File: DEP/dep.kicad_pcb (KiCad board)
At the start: 2 copper layers, 100 x 73 mm, 54 parts, among them J1 AudioJack2, J2 Barrel_Jack_Switch, J3 AudioJack2, J4 AudioJack2, J5 Conn_01x14, J6 Conn_01x14, J7 Conn_01x20, J8 Conn_01x20, U1 OPA2134, U2 PCM4201PWR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

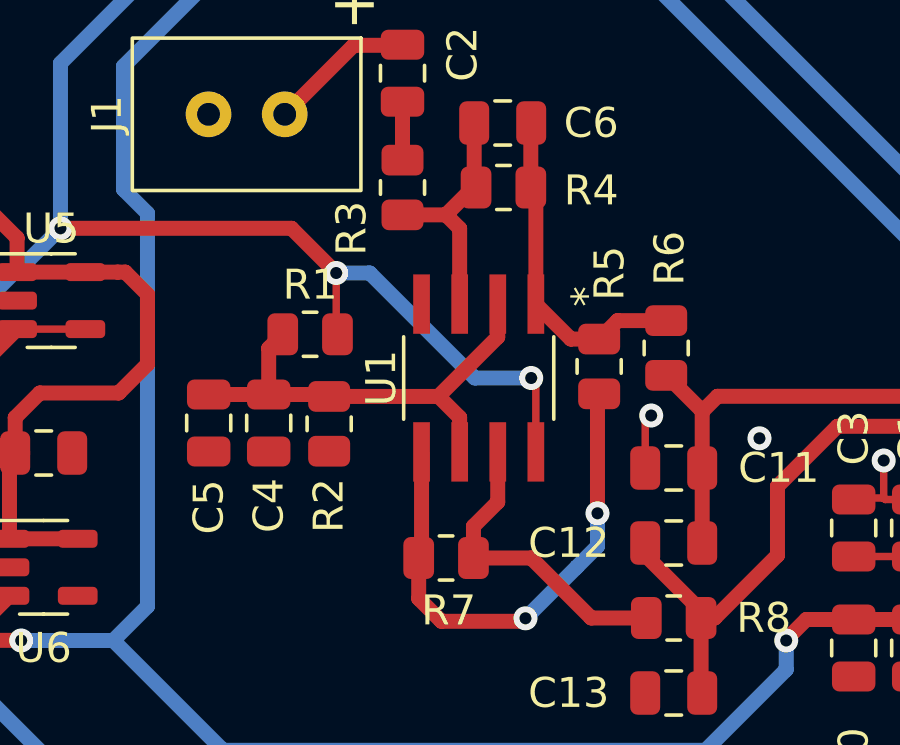
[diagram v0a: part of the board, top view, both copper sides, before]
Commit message: fix +/- op-amp error...
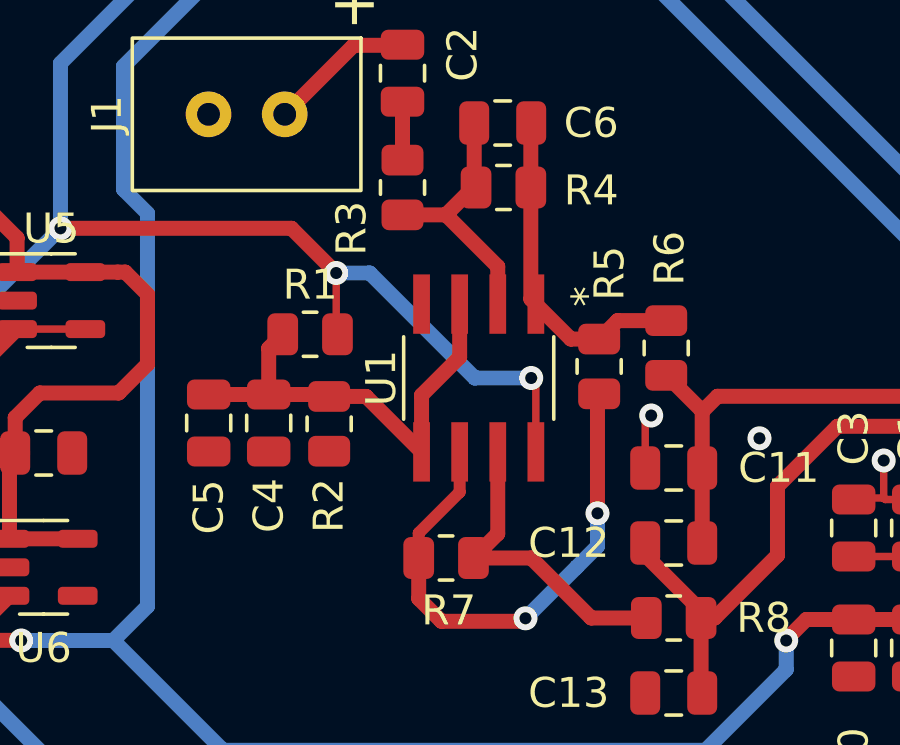
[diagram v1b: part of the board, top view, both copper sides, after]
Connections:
- U1 pad 2: /Input/2V5_reference_input_stage -> /Input/OPamp_1_positive_input
- U1 pad 3: /Input/OPamp_1_positive_input -> /Input/2V5_reference_input_stage
- U1 pad 5: /Input/OPamp_2_positive_input -> /Input/2V5_reference_input_stage
- U1 pad 6: /Input/2V5_reference_input_stage -> /Input/OPamp_2_positive_input
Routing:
- net /Input/OPamp_2_positive_input: track 17.3 -> 18.0 mm
- net /Input/OPamp_1_positive_input: track 8.07 -> 8.59 mm
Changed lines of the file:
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@@
       (net 31 "/Input/OPamp_1_output") (pintype "output"))
     (pad "2" smd rect (at -2.4638 -0.635 270) (size 1.9812 0.5588) (layers "F.Cu" "F.Paste" "F.Mask")
-      (net 29 "/Input/2V5_reference_input_stage") (pinfunction "-") (pintype "input"))
+      (net 30 "/Input/OPamp_1_positive_input") (pinfunction "-") (pintype "input"))
     (pad "3" smd rect (at -2.4638 0.635 270) (size 1.9812 0.5588) (layers "F.Cu" "F.Paste" "F.Mask")
-      (net 30 "/Input/OPamp_1_positive_input") (pinfunction "+") (pintype "input"))
+      (net 29 "/Input/2V5_reference_input_stage") (pinfunction "+") (pintype "input"))
     (pad "4" smd rect (at -2.4638 1.905 270) (size 1.9812 0.5588) (layers "F.Cu" "F.Paste" "F.Mask")
       (net 1 "GND") (pinfunction "V-") (pintype "power_in"))
     (pad "5" smd rect (at 2.4638 1.905 270) (size 1.9812 0.5588) (layers "F.Cu" "F.Paste" "F.Mask")
-      (net 32 "/Input/OPamp_2_positive_input") (pinfunction "+") (pintype "input"))
+      (net 29 "/Input/2V5_reference_input_stage") (pinfunction "+") (pintype "input"))
     (pad "6" smd rect (at 2.4638 0.635 270) (size 1.9812 0.5588) (layers "F.Cu" "F.Paste" "F.Mask")
-      (net 29 "/Input/2V5_reference_input_stage") (pinfunction "-") (pintype "input"))
+      (net 32 "/Input/OPamp_2_positive_input") (pinfunction "-") (pintype "input"))
     (pad "7" smd rect (at 2.4638 -0.635 270) (size 1.9812 0.5588) (layers "F.Cu" "F.Paste" "F.Mask")
       (net 33 "/Input/OPamp_2_output") (pintype "output"))
@@
   (segment (start 128.611 85.96) (end 125.254 85.96) (width 0.5) (layer "F.Cu") (net 28))
   (segment (start 128.86 85.96) (end 129.6 86.7) (width 0.5) (layer "F.Cu") (net 28))
-  (segment (start 140.006 90.806) (end 140.006 91.9538) (width 0.5) (layer "F.Cu") (net 29))
-  (segment (start 139.305 90.095) (end 141.276 88.124) (width 0.5) (layer "F.Cu") (net 29))
-  (segment (start 139.305 90.105) (end 140.006 90.806) (width 0.5) (layer "F.Cu") (net 29))
+  (segment (start 138.736 91.9538) (end 138.736 90.064) (width 0.5) (layer "F.Cu") (net 29))
   (segment (start 135.591 90.04) (end 135.656 90.105) (width 0.5) (layer "F.Cu") (net 29))
-  (segment (start 141.276 88.124) (end 141.276 87.0262) (width 0.5) (layer "F.Cu") (net 29))
-  (segment (start 139.305 90.105) (end 139.305 90.095) (width 0.5) (layer "F.Cu") (net 29))
   (segment (start 133.641 88.5) (end 134.1085 88.0325) (width 0.5) (layer "F.Cu") (net 29))
   (segment (start 133.641 90.04) (end 135.591 90.04) (width 0.5) (layer "F.Cu") (net 29))
+  (segment (start 140.006 88.794) (end 140.006 87.0262) (width 0.5) (layer "F.Cu") (net 29))
   (segment (start 133.641 90.04) (end 133.641 88.5) (width 0.5) (layer "F.Cu") (net 29))
-  (segment (start 135.656 90.105) (end 139.305 90.105) (width 0.5) (layer "F.Cu") (net 29))
+  (segment (start 136.8872 90.105) (end 138.736 91.9538) (width 0.5) (layer "F.Cu") (net 29))
+  (segment (start 138.736 90.064) (end 140.006 88.794) (width 0.5) (layer "F.Cu") (net 29))
+  (segment (start 135.656 90.105) (end 136.8872 90.105) (width 0.5) (layer "F.Cu") (net 29))
   (segment (start 131.641 90.04) (end 133.641 90.04) (width 0.5) (layer "F.Cu") (net 29))
-  (segment (start 140.006 84.506) (end 140.006 87.0262) (width 0.5) (layer "F.Cu") (net 30))
   (segment (start 140.491 80.99) (end 140.491 83.109) (width 0.5) (layer "F.Cu") (net 30))
-  (segment (start 139.5525 84.0525) (end 140.006 84.506) (width 0.5) (layer "F.Cu") (net 30))
+  (segment (start 139.5475 84.0525) (end 139.5525 84.0525) (width 0.5) (layer "F.Cu") (net 30))
+  (segment (start 141.276 85.776) (end 141.276 87.0262) (width 0.5) (layer "F.Cu") (net 30))
   (segment (start 140.491 83.109) (end 139.5475 84.0525) (width 0.5) (layer "F.Cu") (net 30))
   (segment (start 139.5475 84.0525) (end 138.101 84.0525) (width 0.5) (layer "F.Cu") (net 30))
-  (segment (start 139.5475 84.0525) (end 139.5525 84.0525) (width 0.5) (layer "F.Cu") (net 30))
+  (segment (start 139.5525 84.0525) (end 141.276 85.776) (width 0.5) (layer "F.Cu") (net 30))
   (segment (start 142.546 83.3075) (end 142.3785 83.14) (width 0.5) (layer "F.Cu") (net 31))
+  (segment (start 142.3785 83.14) (end 142.3785 86.8587) (width 0.5) (layer "F.Cu") (net 31))
   (segment (start 144.656 88.1925) (end 143.7123 88.1925) (width 0.5) (layer "F.Cu") (net 31))
   (segment (start 142.3785 83.14) (end 142.3785 81.0025) (width 0.5) (layer "F.Cu") (net 31))
   (segment (start 142.3785 81.0025) (end 142.391 80.99) (width 0.5) (layer "F.Cu") (net 31))
   (segment (start 146.891 87.5775) (end 145.271 87.5775) (width 0.5) (layer "F.Cu") (net 31))
-  (segment (start 142.546 87.0262) (end 142.546 83.3075) (width 0.5) (layer "F.Cu") (net 31))
-  (segment (start 143.7123 88.1925) (end 142.546 87.0262) (width 0.5) (layer "F.Cu") (net 31))
+  (segment (start 142.546 87.0262) (end 143.7123 88.1925) (width 0.5) (layer "F.Cu") (net 31))
+  (segment (start 142.3785 86.8587) (end 142.546 87.0262) (width 0.5) (layer "F.Cu") (net 31))
   (segment (start 145.271 87.5775) (end 144.656 88.1925) (width 0.5) (layer "F.Cu") (net 31))
+  (segment (start 140.006 93.294) (end 138.641 94.659) (width 0.4) (layer "F.Cu") (net 32))
   (segment (start 138.641 96.841) (end 139.4 97.6) (width 0.5) (layer "F.Cu") (net 32))
-  (segment (start 138.736 91.9538) (end 138.736 95.395) (width 0.5) (layer "F.Cu") (net 32))
+  (segment (start 138.641 94.659) (end 138.641 95.49) (width 0.4) (layer "F.Cu") (net 32))
   (segment (start 139.4 97.6) (end 142.1 97.6) (width 0.5) (layer "F.Cu") (net 32))
+  (segment (start 140.006 91.9538) (end 140.006 93.294) (width 0.4) (layer "F.Cu") (net 32))
   (segment (start 142.1 97.6) (end 142.2 97.5) (width 0.5) (layer "F.Cu") (net 32))
   (segment (start 144.6 94) (end 144.6 90.0735) (width 0.5) (layer "F.Cu") (net 32))
@@
   (segment (start 142.2 97.5) (end 143.9 95.8) (width 0.5) (layer "B.Cu") (net 32))
   (segment (start 143.9 95.8) (end 144.6 95.1) (width 0.5) (layer "B.Cu") (net 32))
+  (segment (start 141.276 94.68) (end 141.276 91.9538) (width 0.5) (layer "F.Cu") (net 33))
+  (segment (start 140.466 95.49) (end 141.276 94.68) (width 0.5) (layer "F.Cu") (net 33))
   (segment (start 142.391 95.49) (end 144.391 97.49) (width 0.5) (layer "F.Cu") (net 33))
   (segment (start 144.391 97.49) (end 146.2285 97.49) (width 0.5) (layer "F.Cu") (net 33))
   (segment (start 140.466 95.49) (end 142.391 95.49) (width 0.5) (layer "F.Cu") (net 33))
-  (segment (start 141.276 93.624) (end 140.466 94.434) (width 0.5) (layer "F.Cu") (net 33))
-  (segment (start 141.276 91.9538) (end 141.276 93.624) (width 0.5) (layer "F.Cu") (net 33))
-  (segment (start 140.466 94.434) (end 140.466 95.49) (width 0.5) (layer "F.Cu") (net 33))
   (segment (start 181.151 110.495) (end 181.151 116.765) (width 0.25) (layer "F.Cu") (net 34))
   (segment (start 181.151 116.765) (end 181.046 116.87) (width 0.25) (layer "F.Cu") (net 34))
